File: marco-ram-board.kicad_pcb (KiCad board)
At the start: 4 copper layers, 160 x 100 mm, 186 parts, among them J201 PRG_USB, J202 MCU_RST, J203 MCU_BOOT0, J204 FT_TXD, J205 FT_RXD, J206 CONN_JTAG, J301 CONN_MCU_SERIAL, J302 CONN_EXT, J501 MCU_USB, J502 SD_Card, J503 CONN_DISP, J504 RJ45_Amphenol_RJMG1BD3B8K1ANR, J601 CONN_JACK_12V, J602 CONN_SCREW_12V, Q201 MMBT3906, Q601 DMP3037LSS, SW301 SW_RST, SW302 SW_BOOT0, SW501 BTN0, SW502 BTN1, SW503 BTN2, SW504 BTN3, SW601 PWR_SW, U201 FT2232HL, U301 STM32F765IITx, U401 IS42S86400D, U402 IS42S86400D, U403 IS42S86400D, U404 IS42S86400D, U405 IS42S86400D, U406 IS42S86400D, U407 IS42S86400D, U408 IS42S86400D, U501 KSZ8081RNA, U601 LM2576S-3.3, Y201 12MHz, Y301 25MHz

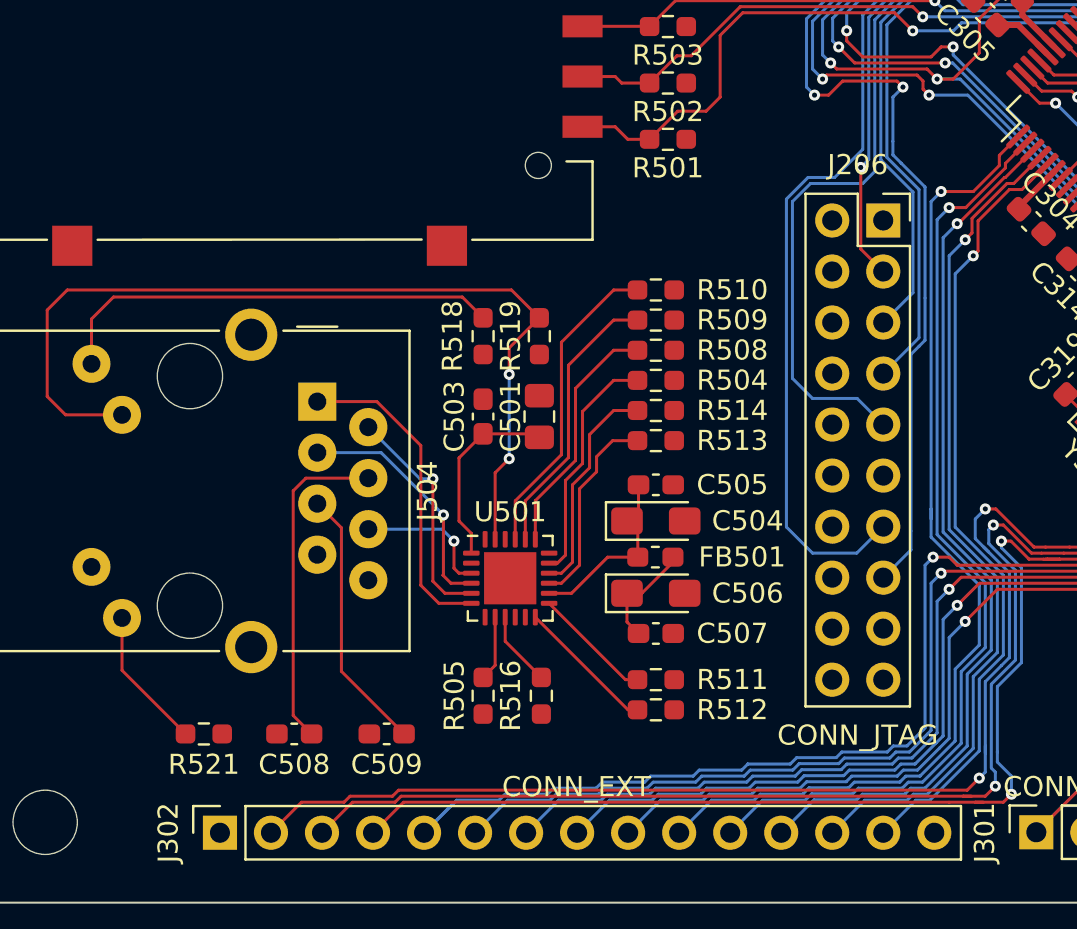
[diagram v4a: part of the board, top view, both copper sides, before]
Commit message: Add names to Ext connector pins.
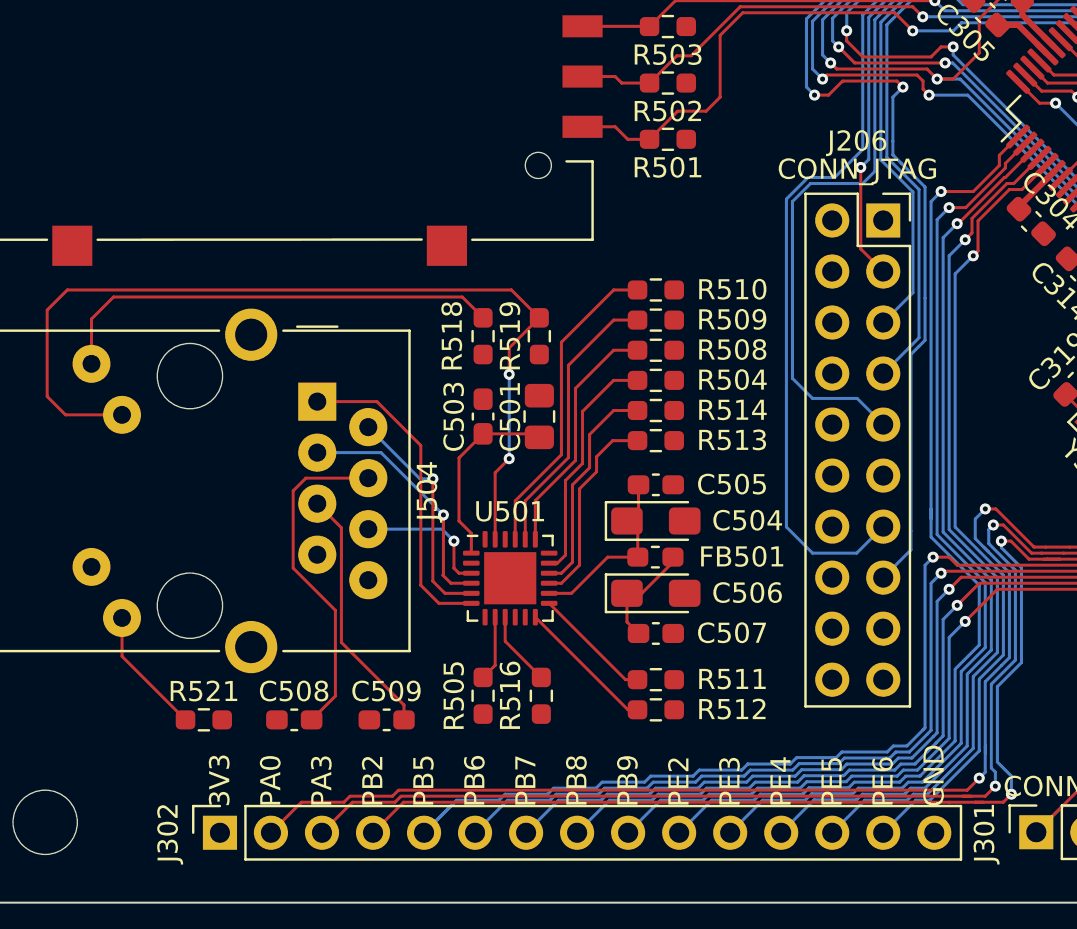
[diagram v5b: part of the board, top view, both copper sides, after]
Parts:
- moved C508 0.70 mm to (86.4, 130.9)
- moved C509 0.70 mm to (91.0, 130.9)
- moved R521 0.70 mm to (81.9, 130.9)
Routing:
- net Net-(J504-PadL1): track 7.08 -> 6.38 mm
- net Net-(C509-Pad1): track 13.3 -> 12.6 mm
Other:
- board text added: "3V3"
- board text added: "GND"
- board text added: "PA0"
- board text added: "PA3"
- board text added: "PB2"
- board text added: "PB5"
- board text added: "PB6"
- board text added: "PB7"
- board text added: "PB8"
- board text added: "PB9"
- board text added: "PE2"
- board text added: "PE3"
- board text added: "PE4"
- board text added: "PE5"
- board text added: "PE6"
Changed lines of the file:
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@@
     (property "Sheetname" "prg-if")
     (attr through_hole)
-    (fp_text reference "J206" (at -1.27 -2.77) (layer "F.SilkS")
+    (fp_text reference "J206" (at -1.27 -3.94) (layer "F.SilkS")
       (effects (font (size 1 1) (thickness 0.15)))
     )
-    (fp_text value "CONN_JTAG" (at -1.27 25.63) (layer "F.SilkS")
+    (fp_text value "CONN_JTAG" (at -1.27 -2.54) (layer "F.SilkS")
       (effects (font (size 1 1) (thickness 0.15)))
     )
@@
   )
   (footprint "Capacitor_SMD:C_0603_1608Metric_Pad1.08x0.95mm_HandSolder" (layer "F.Cu")
-    (at 91 131.6 180)
+    (at 91 130.9 180)
     (descr "Capacitor SMD 0603 (1608 Metric), square (rectangular) end terminal, IPC_7351 nominal with elongated pad for handsoldering. (Body size source: IPC-SM-782 page 76, https://www.pcb-3d.com/wordpress/wp-content/uploads/ipc-sm-782a_amendment_1_and_2.pdf), generated with kicad-footprint-generator")
     (tags "capacitor handsolder")
@@
     (property "Sheetname" "mcu-if")
     (attr smd)
-    (fp_text reference "C509" (at 0 -1.524) (layer "F.SilkS")
+    (fp_text reference "C509" (at 0 1.4) (layer "F.SilkS")
       (effects (font (size 1 1) (thickness 0.15)))
     )
@@
   )
   (footprint "Capacitor_SMD:C_0603_1608Metric_Pad1.08x0.95mm_HandSolder" (layer "F.Cu")
-    (at 86.4 131.6 180)
+    (at 86.4 130.9 180)
     (descr "Capacitor SMD 0603 (1608 Metric), square (rectangular) end terminal, IPC_7351 nominal with elongated pad for handsoldering. (Body size source: IPC-SM-782 page 76, https://www.pcb-3d.com/wordpress/wp-content/uploads/ipc-sm-782a_amendment_1_and_2.pdf), generated with kicad-footprint-generator")
     (tags "capacitor handsolder")
@@
     (property "Sheetname" "mcu-if")
     (attr smd)
-    (fp_text reference "C508" (at 0 -1.524) (layer "F.SilkS")
+    (fp_text reference "C508" (at 0 1.4) (layer "F.SilkS")
       (effects (font (size 1 1) (thickness 0.15)))
     )
@@
       (effects (font (size 1 1) (thickness 0.15)))
     )
-    (fp_text value "CONN_EXT" (at 2.286 17.75 180) (layer "F.SilkS")
+    (fp_text value "CONN_EXT" (at -2.58 17.75 180) (layer "F.Fab")
       (effects (font (size 1 1) (thickness 0.15)))
     )
@@
   )
   (footprint "Resistor_SMD:R_0603_1608Metric_Pad0.98x0.95mm_HandSolder" (layer "F.Cu")
-    (at 81.9 131.6)
+    (at 81.9 130.9)
     (descr "Resistor SMD 0603 (1608 Metric), square (rectangular) end terminal, IPC_7351 nominal with elongated pad for handsoldering. (Body size source: IPC-SM-782 page 72, https://www.pcb-3d.com/wordpress/wp-content/uploads/ipc-sm-782a_amendment_1_and_2.pdf), generated with kicad-footprint-generator")
     (tags "resistor handsolder")
@@
     (property "Sheetname" "mcu-if")
     (attr smd)
-    (fp_text reference "R521" (at 0 1.524) (layer "F.SilkS")
+    (fp_text reference "R521" (at 0 -1.4) (layer "F.SilkS")
       (effects (font (size 1 1) (thickness 0.15)))
     )
@@
   (gr_line (start 70 140) (end 230 140) (layer "Edge.Cuts") (width 0.1))
   (gr_rect (start 219.36 138.402857) (end 186.36 41.402857) (layer "User.1") (width 0.15) (fill none))
+  (gr_text "PB5" (at 92.86 135.25 90) (layer "F.SilkS")
+    (effects (font (size 1 1) (thickness 0.15)) (justify left))
+  )
+  (gr_text "PA3" (at 87.78 135.25 90) (layer "F.SilkS")
+    (effects (font (size 1 1) (thickness 0.15)) (justify left))
+  )
+  (gr_text "PE2" (at 105.56 135.25 90) (layer "F.SilkS")
+    (effects (font (size 1 1) (thickness 0.15)) (justify left))
+  )
+  (gr_text "PE4" (at 110.64 135.25 90) (layer "F.SilkS")
+    (effects (font (size 1 1) (thickness 0.15)) (justify left))
+  )
+  (gr_text "PE3" (at 108.1 135.25 90) (layer "F.SilkS")
+    (effects (font (size 1 1) (thickness 0.15)) (justify left))
+  )
+  (gr_text "GND" (at 118.26 135.25 90) (layer "F.SilkS")
+    (effects (font (size 1 1) (thickness 0.15)) (justify left))
+  )
+  (gr_text "PB9" (at 103.02 135.25 90) (layer "F.SilkS")
+    (effects (font (size 1 1) (thickness 0.15)) (justify left))
+  )
   (gr_text "- 12V +\n" (at 71.905 68.575 270) (layer "F.SilkS")
     (effects (font (size 1.1 1.2) (thickness 0.275)))
   )
+  (gr_text "PB8" (at 100.48 135.25 90) (layer "F.SilkS")
+    (effects (font (size 1 1) (thickness 0.15)) (justify left))
+  )
+  (gr_text "PE6" (at 115.72 135.25 90) (layer "F.SilkS")
+    (effects (font (size 1 1) (thickness 0.15)) (justify left))
+  )
+  (gr_text "PB2" (at 90.32 135.25 90) (layer "F.SilkS")
+    (effects (font (size 1 1) (thickness 0.15)) (justify left))
+  )
   (gr_text "+\n" (at 80.8 47.8 270) (layer "F.SilkS")
     (effects (font (size 1 1) (thickness 0.15)))
   )
+  (gr_text "PA0" (at 85.24 135.25 90) (layer "F.SilkS")
+    (effects (font (size 1 1) (thickness 0.15)) (justify left))
+  )
+  (gr_text "PE5" (at 113.18 135.25 90) (layer "F.SilkS")
+    (effects (font (size 1 1) (thickness 0.15)) (justify left))
+  )
+  (gr_text "3V3" (at 82.7 135.25 90) (layer "F.SilkS")
+    (effects (font (size 1 1) (thickness 0.15)) (justify left))
+  )
+  (gr_text "PB6" (at 95.4 135.25 90) (layer "F.SilkS")
+    (effects (font (size 1 1) (thickness 0.15)) (justify left))
+  )
   (gr_text "-" (at 80.8 41.8 270) (layer "F.SilkS")
     (effects (font (size 1 1) (thickness 0.15)))
   )
+  (gr_text "PB7" (at 97.94 135.25 90) (layer "F.SilkS")
+    (effects (font (size 1 1) (thickness 0.15)) (justify left))
+  )
   (segment (start 215.6 118.3625) (end 213.4 120.5625) (width 0.15) (layer "F.Cu") (net 1))
   (segment (start 142.482501 86.038642) (end 144.954766 83.566377) (width 0.3) (layer "F.Cu") (net 1))
@@
   (segment (start 103.7 124.6) (end 102.9625 124.6) (width 0.15) (layer "F.Cu") (net 14))
   (segment (start 102.9625 126.025) (end 103.5375 126.6) (width 0.15) (layer "F.Cu") (net 14))
-  (segment (start 87.2625 131.6) (end 86.346 130.6835) (width 0.15) (layer "F.Cu") (net 15))
-  (segment (start 86.346 119.499943) (end 86.978943 118.867) (width 0.15) (layer "F.Cu") (net 15))
-  (segment (start 86.978943 118.867) (end 90.086 118.867) (width 0.15) (layer "F.Cu") (net 15))
-  (segment (start 86.346 130.6835) (end 86.346 119.499943) (width 0.15) (layer "F.Cu") (net 15))
-  (segment (start 91.8625 131.6) (end 88.746 128.4835) (width 0.15) (layer "F.Cu") (net 16))
+  (segment (start 88.446 125.446) (end 88.446 129.7165) (width 0.15) (layer "F.Cu") (net 15))
+  (segment (start 88.446 129.7165) (end 87.2625 130.9) (width 0.15) (layer "F.Cu") (net 15))
+  (segment (start 86.346 123.346) (end 88.446 125.446) (width 0.15) (layer "F.Cu") (net 15))
+  (segment (start 90.086 118.867) (end 86.978943 118.867) (width 0.15) (layer "F.Cu") (net 15))
+  (segment (start 86.346 119.499943) (end 86.346 123.346) (width 0.15) (layer "F.Cu") (net 15))
+  (segment (start 86.978943 118.867) (end 86.346 119.499943) (width 0.15) (layer "F.Cu") (net 15))
+  (segment (start 88.746 123.446) (end 88.746 127.046) (width 0.15) (layer "F.Cu") (net 16))
+  (segment (start 88.746 123.446) (end 88.746 121.337) (width 0.15) (layer "F.Cu") (net 16))
   (segment (start 88.746 121.337) (end 87.546 120.137) (width 0.15) (layer "F.Cu") (net 16))
-  (segment (start 88.746 128.4835) (end 88.746 121.337) (width 0.15) (layer "F.Cu") (net 16))
+  (segment (start 88.746 127.046) (end 91.8625 130.1625) (width 0.15) (layer "F.Cu") (net 16))
+  (segment (start 91.8625 130.1625) (end 91.8625 130.9) (width 0.15) (layer "F.Cu") (net 16))
   (segment (start 87.095 61.175) (end 89.635 61.175) (width 0.5) (layer "F.Cu") (net 17))
   (segment (start 88.365 59.835) (end 89.6 58.6) (width 1) (layer "F.Cu") (net 17))
@@
   (segment (start 153.1 83.510052) (end 148.655026 87.955026) (width 0.15) (layer "B.Cu") (net 73))
   (segment (start 148.644974 87.955026) (end 142.2 94.4) (width 0.15) (layer "B.Cu") (net 73))
-  (segment (start 80.9875 131.6) (end 77.826 128.4385) (width 0.15) (layer "F.Cu") (net 74))
-  (segment (start 77.826 128.4385) (end 77.826 125.827) (width 0.15) (layer "F.Cu") (net 74))
+  (segment (start 77.826 125.827) (end 77.826 127.7385) (width 0.15) (layer "F.Cu") (net 74))
+  (segment (start 77.826 127.7385) (end 80.9875 130.9) (width 0.15) (layer "F.Cu") (net 74))
   (segment (start 74.1 114.8) (end 74.1 110.5) (width 0.15) (layer "F.Cu") (net 75))
   (segment (start 98.6 110.8875) (end 97.1 112.3875) (width 0.15) (layer "F.Cu") (net 75))

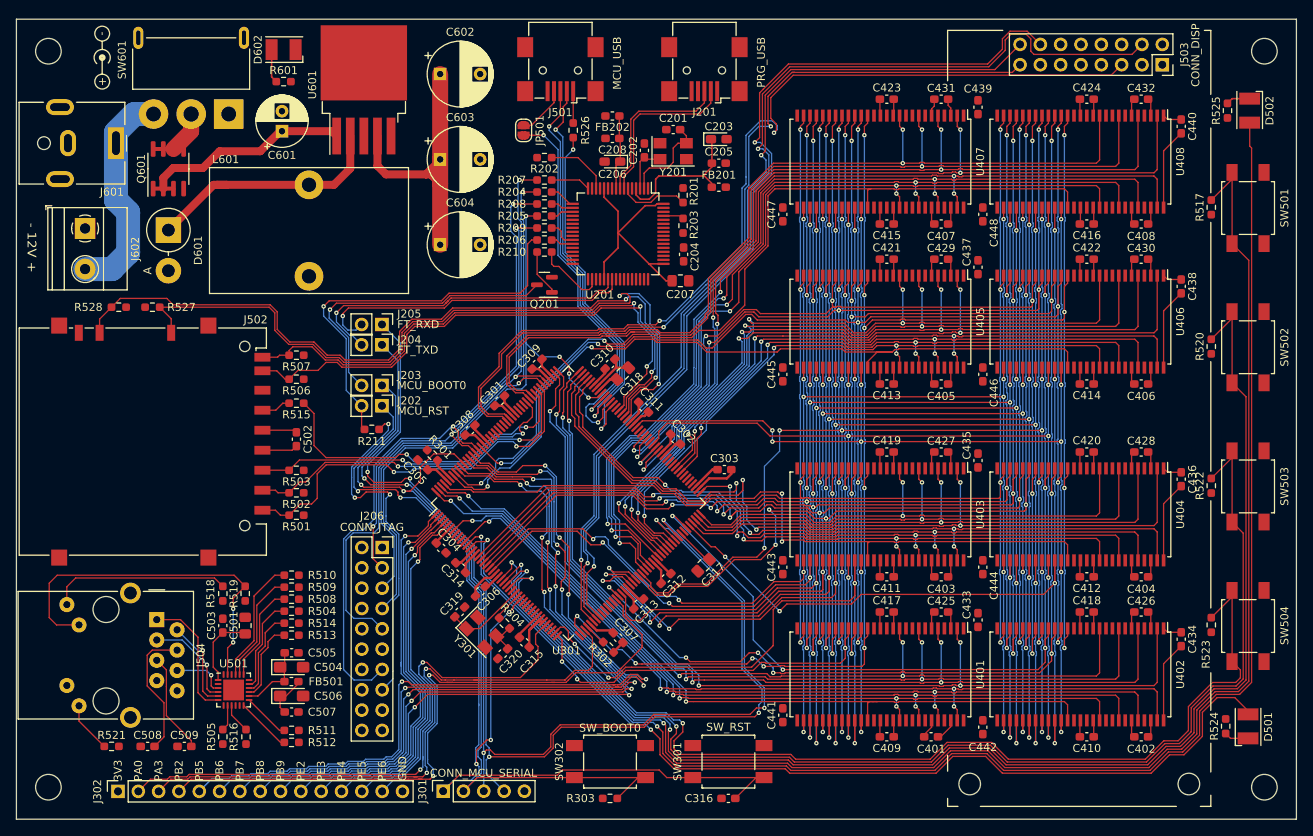
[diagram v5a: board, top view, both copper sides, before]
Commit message: Route RMII.
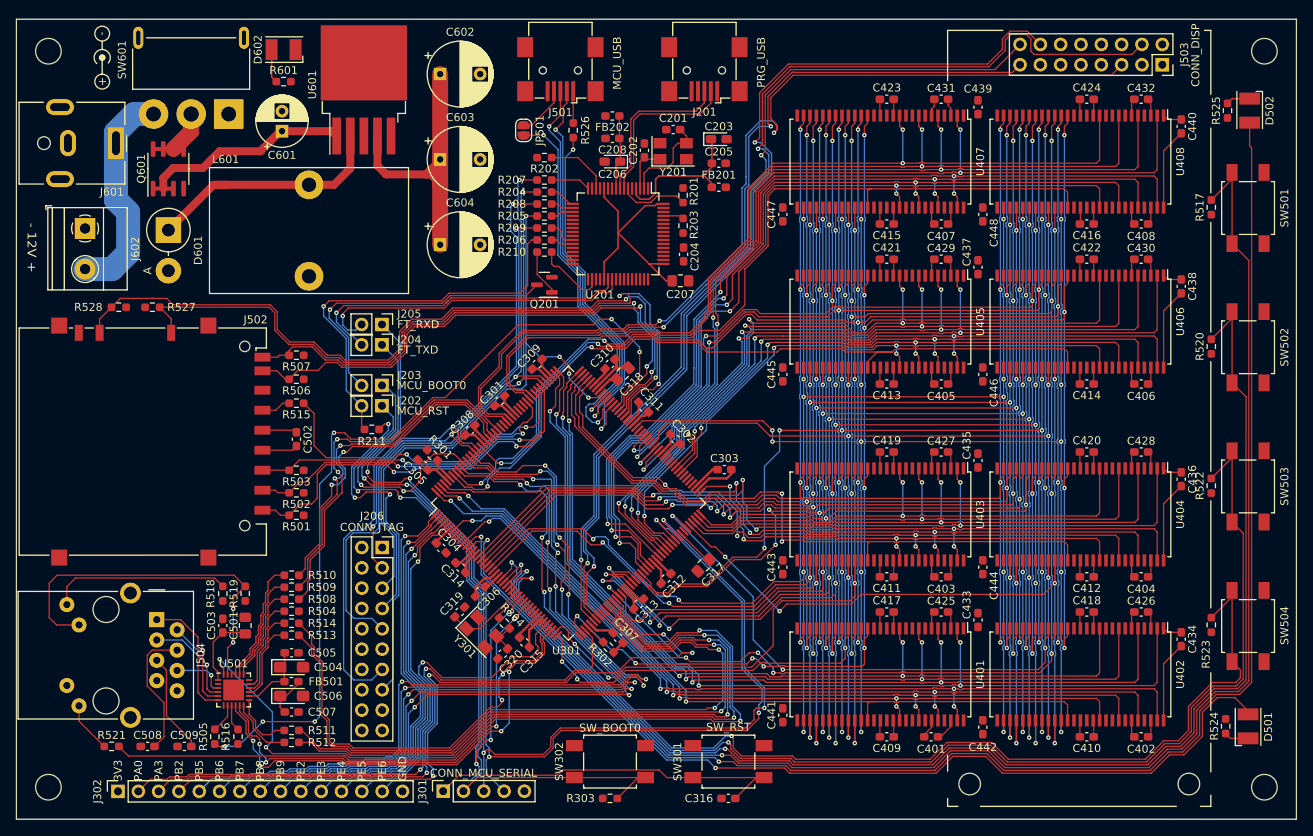
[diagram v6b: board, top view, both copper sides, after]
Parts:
- moved R505 1.00 mm to (94.8, 129.7)
- moved R516 1.00 mm to (97.7, 129.7)
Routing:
- net /mcu-if/RMII.LED: track 0.00 -> 109.3 mm, vias 0 -> 2
- net /mcu-if/RMII.MCO1: track 0.00 -> 105.5 mm, vias 0 -> 6
- net /mcu-if/RMII.~{RST}: track 0.00 -> 105.0 mm, vias 0 -> 4
- net /mcu-if/RMII.CRSDV: track 0.00 -> 91.2 mm, vias 0 -> 2
- net /mcu-if/RMII.RXD1: track 0.00 -> 83.1 mm, vias 0 -> 2
- net /mcu-if/RMII.RXD0: track 0.00 -> 81.7 mm, vias 0 -> 2
- net /mcu-if/RMII.MDIO: track 0.00 -> 58.2 mm, vias 0 -> 4
- net /mcu-if/RMII.MDC: track 0.00 -> 56.7 mm, vias 0 -> 4
- net /mcu-if/RMII.REFCLK: track 0.00 -> 54.3 mm, vias 0 -> 2
- net /mcu-if/RMII.TXEN: track 0.00 -> 46.7 mm, vias 0 -> 2
- net /mcu-if/RMII.TXD0: track 0.00 -> 44.6 mm, vias 0 -> 2
- net /mcu-if/RMII.TXD1: track 0.00 -> 42.0 mm, vias 0 -> 2
- net /mcu/EXT3: track 84.1 -> 94.2 mm, vias 2 -> 4
- net Net-(R511-Pad2): track 5.97 -> 7.98 mm
- net /mcu-if/BTN0: track 186.6 -> 184.7 mm
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
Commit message: Route VDD.
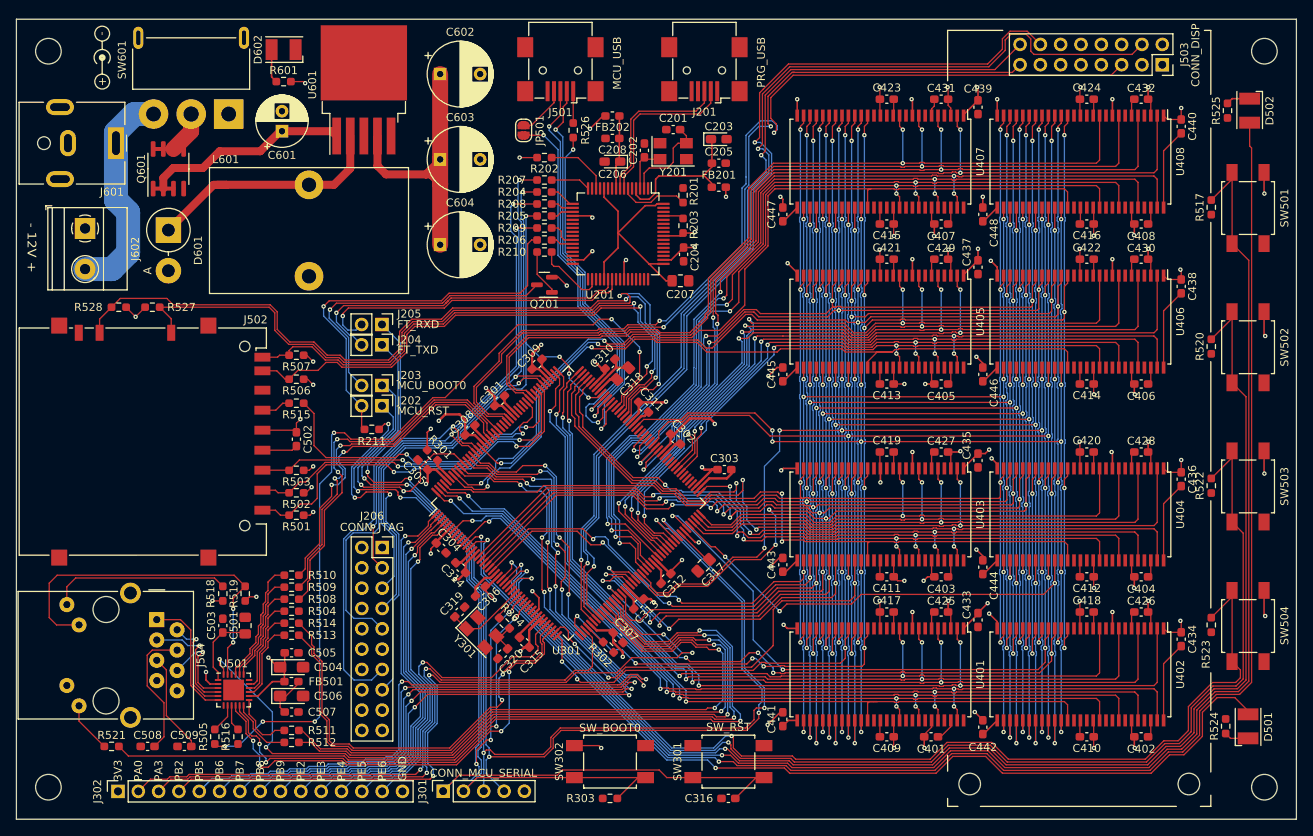
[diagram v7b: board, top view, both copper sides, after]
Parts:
- moved C441 0.50 mm to (165.8, 127.5)
- moved C443 0.30 mm to (165.8, 108.2)
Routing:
- net VDD: track 163.2 -> 392.3 mm, vias 0 -> 108
- net GND: track 148.0 -> 165.9 mm
- net Net-(J504-PadR6): track 6.83 -> 11.0 mm
- net Net-(J504-PadR3): track 12.2 -> 13.9 mm
- net Net-(J504-PadR2): track 11.5 -> 12.4 mm
- net /mcu/SDRAM.A12: track 198.2 -> 199.0 mm
- net /mcu/SDRAM.CLK: track 197.8 -> 198.6 mm
- added copper zone on In1.Cu, net VDD
